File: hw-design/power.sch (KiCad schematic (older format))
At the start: 9 parts

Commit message: Routing
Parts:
- D5, D6: renamed from D?; footprint (none) -> w_smd_diode:do214ac
- U4: renamed from U?; footprint TO_SOT_Packages_SMD:SOT-223 -> linear:SOT223
- gave numbers to parts that had none: 6
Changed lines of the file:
@@
 $EndDescr
 $Comp
-L CP C?
+L CP C15
 U 1 1 5723EAD0
 P 8175 3300
-F 0 "C?" H 8200 3400 50  0000 L CNN
+F 0 "C15" H 8200 3400 50  0000 L CNN
 F 1 "10µF" H 8200 3200 50  0000 L CNN
 F 2 "w_smd_cap:c_tant_B" H 8213 3150 30  0001 C CNN
@@
 	8175 3025 8175 3150
 $Comp
-L MCP73833 U?
+L MCP73833 U3
 U 1 1 5723EAD1
 P 5450 3525
-F 0 "U?" H 5500 3625 60  0000 C CNN
+F 0 "U3" H 5500 3625 60  0000 C CNN
 F 1 "MCP73833" V 5400 3525 60  0000 C CNN
 F 2 "ref-packages:MSOP10" H 5500 3575 60  0001 C CNN
@@
 $EndComp
 $Comp
-L CP C?
+L CP C14
 U 1 1 5723EAD2
 P 7225 3300
-F 0 "C?" H 7343 3346 50  0000 L CNN
+F 0 "C14" H 7343 3346 50  0000 L CNN
 F 1 "10µF" H 7343 3254 50  0000 L CNN
 F 2 "w_smd_cap:c_tant_B" H 7263 3150 30  0001 C CNN
@@
 	3225 3325 4850 3325
 $Comp
-L CP C?
+L CP C13
 U 1 1 5723EAD3
 P 3400 3600
-F 0 "C?" H 3518 3646 50  0000 L CNN
+F 0 "C13" H 3518 3646 50  0000 L CNN
 F 1 "10µF" H 3518 3554 50  0000 L CNN
 F 2 "w_smd_cap:c_tant_B" H 3438 3450 30  0001 C CNN
@@
 	3400 3325 3400 3450
 $Comp
-L +5V #PWR?
+L +5V #PWR022
 U 1 1 5723EAD4
 P 3225 3325
-F 0 "#PWR?" H 3225 3175 50  0001 C CNN
+F 0 "#PWR022" H 3225 3175 50  0001 C CNN
 F 1 "+5V" H 3225 3465 50  0000 C CNN
 F 2 "" H 3225 3325 60  0000 C CNN
@@
 Connection ~ 3400 3325
 $Comp
-L GND #PWR?
+L GND #PWR023
 U 1 1 5723EAD5
 P 3400 3825
-F 0 "#PWR?" H 3400 3575 50  0001 C CNN
+F 0 "#PWR023" H 3400 3575 50  0001 C CNN
 F 1 "GND" H 3400 3675 50  0000 C CNN
 F 2 "" H 3400 3825 60  0000 C CNN
@@
 	4175 3625 4850 3625
 $Comp
-L GND #PWR?
+L GND #PWR024
 U 1 1 5723EAD6
 P 4775 4125
-F 0 "#PWR?" H 4775 3875 50  0001 C CNN
+F 0 "#PWR024" H 4775 3875 50  0001 C CNN
 F 1 "GND" H 4775 3975 50  0000 C CNN
 F 2 "" H 4775 4125 60  0000 C CNN
@@
 	4775 3725 4775 4125
 $Comp
-L GND #PWR?
+L GND #PWR025
 U 1 1 5723EAD7
 P 7750 3750
-F 0 "#PWR?" H 7750 3500 50  0001 C CNN
+F 0 "#PWR025" H 7750 3500 50  0001 C CNN
 F 1 "GND" H 7750 3600 50  0000 C CNN
 F 2 "" H 7750 3750 60  0000 C CNN
@@
 Connection ~ 7750 3525
 $Comp
-L +3V3 #PWR?
+L +3V3 #PWR026
 U 1 1 5723EAD8
 P 8350 3025
-F 0 "#PWR?" H 8350 2875 50  0001 C CNN
+F 0 "#PWR026" H 8350 2875 50  0001 C CNN
 F 1 "+3V3" H 8350 3165 50  0000 C CNN
 F 2 "" H 8350 3025 60  0000 C CNN
@@
 Connection ~ 8175 3025
 $Comp
-L R R?
+L R R12
 U 1 1 5723EAD9
 P 5450 3950
-F 0 "R?" V 5530 3950 50  0000 C CNN
+F 0 "R12" V 5530 3950 50  0000 C CNN
 F 1 "3k3" V 5450 3950 50  0000 C CNN
 F 2 "w_smd_resistors:r_0603" V 5380 3950 30  0001 C CNN
@@
 300mA
 $Comp
-L CONN_01X03 P?
+L CONN_01X03 P3
 U 1 1 5723EADA
 P 6750 3425
-F 0 "P?" V 6715 3231 50  0000 R CNN
+F 0 "P3" V 6715 3231 50  0000 R CNN
 F 1 "CONN_01X03" V 6623 3231 50  0000 R CNN
 F 2 "w_pin_strip:pin_strip_3" H 6750 3425 60  0001 C CNN
@@
 Connection ~ 6125 3325
 $Comp
-L GND #PWR?
+L GND #PWR027
 U 1 1 5723EADB
 P 6550 3575
-F 0 "#PWR?" H 6550 3325 50  0001 C CNN
+F 0 "#PWR027" H 6550 3325 50  0001 C CNN
 F 1 "GND" H 6644 3538 50  0000 L CNN
 F 2 "" H 6550 3575 60  0000 C CNN
@@
 	6550 3575 6550 3525
 $Comp
-L AP111733 U?
+L AP111733 U4
 U 1 1 57241BB2
 P 7750 3025
-F 0 "U?" H 7750 3392 50  0000 C CNN
+F 0 "U4" H 7750 3392 50  0000 C CNN
 F 1 "AP111733" H 7750 3301 50  0000 C CNN
-F 2 "TO_SOT_Packages_SMD:SOT-223" H 7750 2675 50  0001 C CNN
+F 2 "linear:SOT223" H 7750 2675 50  0001 C CNN
 F 3 "" H 7850 2775 50  0000 C CNN
 	1    7750 3025
@@
 	6300 3425 6550 3425
 $Comp
-L D_Schottky D?
+L D_Schottky D6
 U 1 1 57249FBF
 P 6400 3025
-F 0 "D?" H 6400 2809 50  0000 C CNN
+F 0 "D6" H 6400 2809 50  0000 C CNN
 F 1 "D_Schottky" H 6400 2900 50  0000 C CNN
-F 2 "" H 6400 3025 50  0000 C CNN
+F 2 "w_smd_diode:do214ac" H 6400 3025 50  0001 C CNN
 F 3 "" H 6400 3025 50  0000 C CNN
 	1    6400 3025
@@
 	5600 3025 6250 3025
 $Comp
-L D_Schottky D?
+L D_Schottky D5
 U 1 1 5724AD72
 P 6400 2700
-F 0 "D?" H 6400 2484 50  0000 C CNN
+F 0 "D5" H 6400 2484 50  0000 C CNN
 F 1 "D_Schottky" H 6400 2575 50  0000 C CNN
-F 2 "" H 6400 2700 50  0000 C CNN
+F 2 "w_smd_diode:do214ac" H 6400 2700 50  0001 C CNN
 F 3 "" H 6400 2700 50  0000 C CNN
 	1    6400 2700
@@
 sense
 $Comp
-L +BATT #PWR?
+L +BATT #PWR028
 U 1 1 572542F4
 P 6125 2950
-F 0 "#PWR?" H 6125 2800 50  0001 C CNN
+F 0 "#PWR028" H 6125 2800 50  0001 C CNN
 F 1 "+BATT" H 6140 3123 50  0000 C CNN
 F 2 "" H 6125 2950 50  0000 C CNN

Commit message: Mounting holes for additional wheels or whatever
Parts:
- removed D6: D_Schottky, w_smd_diode:do214ac, symbol D_Schottky
- D5: footprint w_smd_diode:do214ac -> iwasz:sod123-pins21
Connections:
- net +BATT: now also C14.1, D5.1 (K), U4.3 (VI)
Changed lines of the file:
@@
 	3400 3325 3400 3450
 $Comp
-L +5V #PWR022
+L +5V #PWR22
 U 1 1 5723EAD4
 P 3225 3325
-F 0 "#PWR022" H 3225 3175 50  0001 C CNN
+F 0 "#PWR22" H 3225 3175 50  0001 C CNN
 F 1 "+5V" H 3225 3465 50  0000 C CNN
 F 2 "" H 3225 3325 60  0000 C CNN
@@
 Connection ~ 3400 3325
 $Comp
-L GND #PWR023
+L GND #PWR23
 U 1 1 5723EAD5
 P 3400 3825
-F 0 "#PWR023" H 3400 3575 50  0001 C CNN
+F 0 "#PWR23" H 3400 3575 50  0001 C CNN
 F 1 "GND" H 3400 3675 50  0000 C CNN
 F 2 "" H 3400 3825 60  0000 C CNN
@@
 	4175 3625 4850 3625
 $Comp
-L GND #PWR024
+L GND #PWR24
 U 1 1 5723EAD6
 P 4775 4125
-F 0 "#PWR024" H 4775 3875 50  0001 C CNN
+F 0 "#PWR24" H 4775 3875 50  0001 C CNN
 F 1 "GND" H 4775 3975 50  0000 C CNN
 F 2 "" H 4775 4125 60  0000 C CNN
@@
 	4775 3725 4775 4125
 $Comp
-L GND #PWR025
+L GND #PWR27
 U 1 1 5723EAD7
 P 7750 3750
-F 0 "#PWR025" H 7750 3500 50  0001 C CNN
+F 0 "#PWR27" H 7750 3500 50  0001 C CNN
 F 1 "GND" H 7750 3600 50  0000 C CNN
 F 2 "" H 7750 3750 60  0000 C CNN
@@
 Connection ~ 7750 3525
 $Comp
-L +3V3 #PWR026
+L +3V3 #PWR28
 U 1 1 5723EAD8
 P 8350 3025
-F 0 "#PWR026" H 8350 2875 50  0001 C CNN
+F 0 "#PWR28" H 8350 2875 50  0001 C CNN
 F 1 "+3V3" H 8350 3165 50  0000 C CNN
 F 2 "" H 8350 3025 60  0000 C CNN
@@
 Connection ~ 6125 3325
 $Comp
-L GND #PWR027
+L GND #PWR26
 U 1 1 5723EADB
 P 6550 3575
-F 0 "#PWR027" H 6550 3325 50  0001 C CNN
+F 0 "#PWR26" H 6550 3325 50  0001 C CNN
 F 1 "GND" H 6644 3538 50  0000 L CNN
 F 2 "" H 6550 3575 60  0000 C CNN
@@
 	6000 3325 6550 3325
 Wire Wire Line
-	6550 3025 7450 3025
+	5600 3025 7450 3025
 Wire Wire Line
 	6550 3575 6550 3525
@@
 	6300 3425 6550 3425
 $Comp
-L D_Schottky D6
-U 1 1 57249FBF
-P 6400 3025
-F 0 "D6" H 6400 2809 50  0000 C CNN
-F 1 "D_Schottky" H 6400 2900 50  0000 C CNN
-F 2 "w_smd_diode:do214ac" H 6400 3025 50  0001 C CNN
-F 3 "" H 6400 3025 50  0000 C CNN
-	1    6400 3025
-	-1   0    0    1
-$EndComp
-Wire Wire Line
-	5600 3025 6250 3025
-$Comp
 L D_Schottky D5
 U 1 1 5724AD72
@@
 F 0 "D5" H 6400 2484 50  0000 C CNN
 F 1 "D_Schottky" H 6400 2575 50  0000 C CNN
-F 2 "w_smd_diode:do214ac" H 6400 2700 50  0001 C CNN
+F 2 "iwasz:sod123-pins21" H 6400 2700 50  0001 C CNN
 F 3 "" H 6400 2700 50  0000 C CNN
 	1    6400 2700
@@
 sense
 $Comp
-L +BATT #PWR028
+L +BATT #PWR25
 U 1 1 572542F4
 P 6125 2950
-F 0 "#PWR028" H 6125 2800 50  0001 C CNN
+F 0 "#PWR25" H 6125 2800 50  0001 C CNN
 F 1 "+BATT" H 6140 3123 50  0000 C CNN
 F 2 "" H 6125 2950 50  0000 C CNN

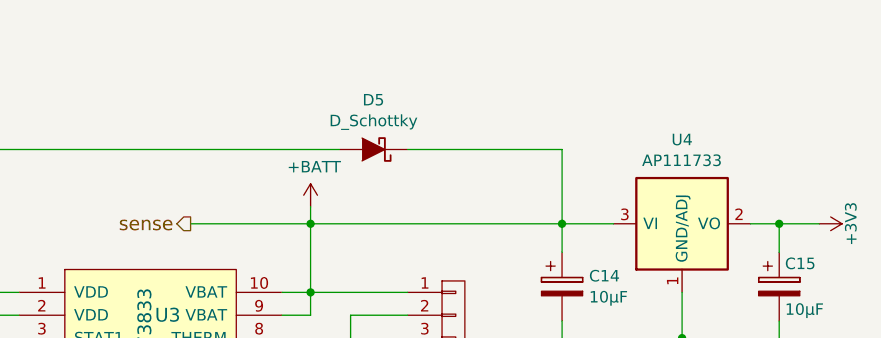
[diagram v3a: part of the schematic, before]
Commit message: Docs, PCB modified (problems with RF and low speed oscillator)
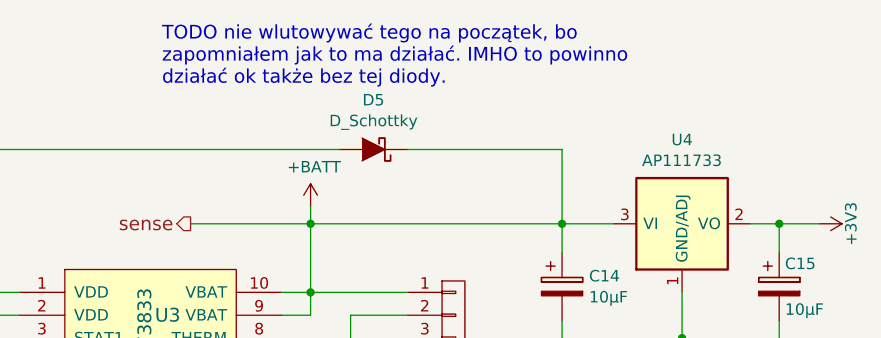
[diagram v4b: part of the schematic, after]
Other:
- note added: "TODO nie wlutowywać tego na początek, bo\nzapomniałem jak to ma działać. IMHO to powinno\ndziałać ok także bez tej diody."
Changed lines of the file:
@@
 	3400 3325 3400 3450
 $Comp
-L +5V #PWR22
+L +5V #PWR022
 U 1 1 5723EAD4
 P 3225 3325
-F 0 "#PWR22" H 3225 3175 50  0001 C CNN
+F 0 "#PWR022" H 3225 3175 50  0001 C CNN
 F 1 "+5V" H 3225 3465 50  0000 C CNN
 F 2 "" H 3225 3325 60  0000 C CNN
@@
 Connection ~ 3400 3325
 $Comp
-L GND #PWR23
+L GND #PWR023
 U 1 1 5723EAD5
 P 3400 3825
-F 0 "#PWR23" H 3400 3575 50  0001 C CNN
+F 0 "#PWR023" H 3400 3575 50  0001 C CNN
 F 1 "GND" H 3400 3675 50  0000 C CNN
 F 2 "" H 3400 3825 60  0000 C CNN
@@
 	4175 3625 4850 3625
 $Comp
-L GND #PWR24
+L GND #PWR024
 U 1 1 5723EAD6
 P 4775 4125
-F 0 "#PWR24" H 4775 3875 50  0001 C CNN
+F 0 "#PWR024" H 4775 3875 50  0001 C CNN
 F 1 "GND" H 4775 3975 50  0000 C CNN
 F 2 "" H 4775 4125 60  0000 C CNN
@@
 	4775 3725 4775 4125
 $Comp
-L GND #PWR27
+L GND #PWR025
 U 1 1 5723EAD7
 P 7750 3750
-F 0 "#PWR27" H 7750 3500 50  0001 C CNN
+F 0 "#PWR025" H 7750 3500 50  0001 C CNN
 F 1 "GND" H 7750 3600 50  0000 C CNN
 F 2 "" H 7750 3750 60  0000 C CNN
@@
 Connection ~ 7750 3525
 $Comp
-L +3V3 #PWR28
+L +3V3 #PWR026
 U 1 1 5723EAD8
 P 8350 3025
-F 0 "#PWR28" H 8350 2875 50  0001 C CNN
+F 0 "#PWR026" H 8350 2875 50  0001 C CNN
 F 1 "+3V3" H 8350 3165 50  0000 C CNN
 F 2 "" H 8350 3025 60  0000 C CNN
@@
 Connection ~ 6125 3325
 $Comp
-L GND #PWR26
+L GND #PWR027
 U 1 1 5723EADB
 P 6550 3575
-F 0 "#PWR26" H 6550 3325 50  0001 C CNN
+F 0 "#PWR027" H 6550 3325 50  0001 C CNN
 F 1 "GND" H 6644 3538 50  0000 L CNN
 F 2 "" H 6550 3575 60  0000 C CNN
@@
 sense
 $Comp
-L +BATT #PWR25
+L +BATT #PWR028
 U 1 1 572542F4
 P 6125 2950
-F 0 "#PWR25" H 6125 2800 50  0001 C CNN
+F 0 "#PWR028" H 6125 2800 50  0001 C CNN
 F 1 "+BATT" H 6140 3123 50  0000 C CNN
 F 2 "" H 6125 2950 50  0000 C CNN
@@
 	1    0    0    -1
 $EndComp
+Text Notes 5475 2425 0    60   ~ 0
+TODO nie wlutowywać tego na początek, bo\nzapomniałem jak to ma działać. IMHO to powinno\ndziałać ok także bez tej diody.
 $EndSCHEMATC

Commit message: Gerbery 1.1
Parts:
- added P10: CONN_01X02, w_pin_strip:pin_strip_2, symbol CONN_01X02
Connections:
- net +BATT: now also P10.1 (P1); no longer P3.1 (P1), U3.10 (VBAT), U3.9 (VBAT)
- new net: P10.2 (P2), P3.1 (P1), U3.10 (VBAT), U3.9 (VBAT)
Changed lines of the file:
@@
 	3400 3325 3400 3450
 $Comp
-L +5V #PWR022
+L +5V #PWR22
 U 1 1 5723EAD4
 P 3225 3325
-F 0 "#PWR022" H 3225 3175 50  0001 C CNN
+F 0 "#PWR22" H 3225 3175 50  0001 C CNN
 F 1 "+5V" H 3225 3465 50  0000 C CNN
 F 2 "" H 3225 3325 60  0000 C CNN
@@
 Connection ~ 3400 3325
 $Comp
-L GND #PWR023
+L GND #PWR23
 U 1 1 5723EAD5
 P 3400 3825
-F 0 "#PWR023" H 3400 3575 50  0001 C CNN
+F 0 "#PWR23" H 3400 3575 50  0001 C CNN
 F 1 "GND" H 3400 3675 50  0000 C CNN
 F 2 "" H 3400 3825 60  0000 C CNN
@@
 	4175 3625 4850 3625
 $Comp
-L GND #PWR024
+L GND #PWR24
 U 1 1 5723EAD6
 P 4775 4125
-F 0 "#PWR024" H 4775 3875 50  0001 C CNN
+F 0 "#PWR24" H 4775 3875 50  0001 C CNN
 F 1 "GND" H 4775 3975 50  0000 C CNN
 F 2 "" H 4775 4125 60  0000 C CNN
@@
 	4775 3725 4775 4125
 $Comp
-L GND #PWR025
+L GND #PWR27
 U 1 1 5723EAD7
 P 7750 3750
-F 0 "#PWR025" H 7750 3500 50  0001 C CNN
+F 0 "#PWR27" H 7750 3500 50  0001 C CNN
 F 1 "GND" H 7750 3600 50  0000 C CNN
 F 2 "" H 7750 3750 60  0000 C CNN
@@
 Connection ~ 7750 3525
 $Comp
-L +3V3 #PWR026
+L +3V3 #PWR28
 U 1 1 5723EAD8
 P 8350 3025
-F 0 "#PWR026" H 8350 2875 50  0001 C CNN
+F 0 "#PWR28" H 8350 2875 50  0001 C CNN
 F 1 "+3V3" H 8350 3165 50  0000 C CNN
 F 2 "" H 8350 3025 60  0000 C CNN
@@
 Connection ~ 6125 3325
 $Comp
-L GND #PWR027
+L GND #PWR26
 U 1 1 5723EADB
 P 6550 3575
-F 0 "#PWR027" H 6550 3325 50  0001 C CNN
+F 0 "#PWR26" H 6550 3325 50  0001 C CNN
 F 1 "GND" H 6644 3538 50  0000 L CNN
 F 2 "" H 6550 3575 60  0000 C CNN
@@
 Connection ~ 7225 3025
 Wire Wire Line
-	6125 2950 6125 3425
+	6125 2950 6125 3125
+Wire Wire Line
+	6125 3225 6125 3425
 Wire Wire Line
 	6300 3425 6300 3525
-Wire Wire Line
-	6000 3325 6550 3325
 Wire Wire Line
 	5600 3025 7450 3025
@@
 sense
 $Comp
-L +BATT #PWR028
+L +BATT #PWR25
 U 1 1 572542F4
 P 6125 2950
-F 0 "#PWR028" H 6125 2800 50  0001 C CNN
+F 0 "#PWR25" H 6125 2800 50  0001 C CNN
 F 1 "+BATT" H 6140 3123 50  0000 C CNN
 F 2 "" H 6125 2950 50  0000 C CNN
@@
 Text Notes 5475 2425 0    60   ~ 0
 TODO nie wlutowywać tego na początek, bo\nzapomniałem jak to ma działać. IMHO to powinno\ndziałać ok także bez tej diody.
+$Comp
+L CONN_01X02 P10
+U 1 1 577EA8A3
+P 6350 3175
+F 0 "P10" H 6428 3216 50  0000 L CNN
+F 1 "CONN_01X02" H 6428 3125 50  0000 L CNN
+F 2 "w_pin_strip:pin_strip_2" V 6178 3037 50  0001 R CNN
+F 3 "" H 6350 3175 50  0000 C CNN
+	1    6350 3175
+	1    0    0    -1
+$EndComp
+Wire Wire Line
+	6000 3325 6550 3325
+Wire Wire Line
+	6125 3125 6150 3125
+Wire Wire Line
+	6125 3225 6150 3225
 $EndSCHEMATC

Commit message: BT turned of/on #define
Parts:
- U3: Datasheet2 (none) -> http://pl.rs-online.com/web/p/uklady-ladowania-akumulatorow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
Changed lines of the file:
@@
 F 2 "ref-packages:MSOP10" H 5500 3575 60  0001 C CNN
 F 3 "http://pl.farnell.com/microchip/mcp73833-fci-un/ic-charge-control-li-ion-1a-msop/dp/1605576" H 5500 3575 60  0001 C CNN
+F 4 "http://pl.rs-online.com/web/p/uklady-ladowania-akumulatorow/7240523/" H 5450 3525 60  0001 C CNN "Datasheet2"
 	1    5450 3525
 	1    0    0    -1

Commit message: version 1.1 works.
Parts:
- removed D5: D_Schottky, iwasz:sod123-pins21, symbol D_Schottky
- added R18: 10k, w_smd_resistors:r_0603, symbol R
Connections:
- net GND: now also R18.1
- net at P3.2 (P2), U3.8 (THERM): now also R18.2
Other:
- note added: "300mA, 4k7 = 210mA, Ireg = 1000V/Rreg\nGdy bateria nie ma termometru, to wlutować R18"
- note added: "opt"
- note removed: "300mA"
- note removed: "TODO nie wlutowywać tego na początek, bo\nzapomniałem jak to ma działać. IMHO to powinno\ndziałać ok także bez tej diody."
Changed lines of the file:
@@
 Wire Wire Line
 	4675 3425 4850 3425
-Wire Wire Line
-	4675 2700 4675 3425
 Connection ~ 4675 3325
 Wire Wire Line
@@
 	4775 3950 5300 3950
 Connection ~ 4775 3950
-Text Notes 5300 4150 0    60   ~ 0
-300mA
+Text Notes 4375 4575 0    60   ~ 0
+300mA, 4k7 = 210mA, Ireg = 1000V/Rreg\nGdy bateria nie ma termometru, to wlutować R18
 $Comp
 L CONN_01X03 P3
@@
 L GND #PWR26
 U 1 1 5723EADB
-P 6550 3575
-F 0 "#PWR26" H 6550 3325 50  0001 C CNN
-F 1 "GND" H 6644 3538 50  0000 L CNN
-F 2 "" H 6550 3575 60  0000 C CNN
-F 3 "" H 6550 3575 60  0000 C CNN
-	1    6550 3575
+P 6550 4025
+F 0 "#PWR26" H 6550 3775 50  0001 C CNN
+F 1 "GND" H 6644 3988 50  0000 L CNN
+F 2 "" H 6550 4025 60  0000 C CNN
+F 3 "" H 6550 4025 60  0000 C CNN
+	1    6550 4025
 	1    0    0    -1
 $EndComp
@@
 	6125 3225 6125 3425
 Wire Wire Line
-	6300 3425 6300 3525
+	6300 3425 6300 3575
 Wire Wire Line
-	5600 3025 7450 3025
-Wire Wire Line
-	6550 3575 6550 3525
+	6550 3525 6550 4025
 $Comp
 L AP111733 U4
@@
 	1    0    0    -1
 $EndComp
-Wire Wire Line
-	7225 2700 7225 3150
 NoConn ~ 6000 3625
 Wire Wire Line
 	6300 3425 6550 3425
-$Comp
-L D_Schottky D5
-U 1 1 5724AD72
-P 6400 2700
-F 0 "D5" H 6400 2484 50  0000 C CNN
-F 1 "D_Schottky" H 6400 2575 50  0000 C CNN
-F 2 "iwasz:sod123-pins21" H 6400 2700 50  0001 C CNN
-F 3 "http://pl.farnell.com/multicomp/1n4148ws/diode-h-speed-100v-0-15a-sod323/dp/1466524" H 6400 2700 50  0001 C CNN
-	1    6400 2700
-	-1   0    0    1
-$EndComp
-Wire Wire Line
-	4675 2700 6250 2700
-Wire Wire Line
-	6550 2700 7225 2700
 Connection ~ 6125 3025
 Text HLabel 4175 3525 0    60   Output ~ 0
@@
 Text HLabel 4175 3625 0    60   Output ~ 0
 complete
-Text HLabel 5600 3025 0    60   Output ~ 0
+Text HLabel 7225 2850 1    60   Output ~ 0
 sense
 $Comp
@@
 	1    0    0    -1
 $EndComp
-Text Notes 5475 2425 0    60   ~ 0
-TODO nie wlutowywać tego na początek, bo\nzapomniałem jak to ma działać. IMHO to powinno\ndziałać ok także bez tej diody.
 $Comp
 L CONN_01X02 P10
@@
 Wire Wire Line
 	6125 3225 6150 3225
+$Comp
+L R R18
+U 1 1 57D567E4
+P 6300 3725
+F 0 "R18" V 6380 3725 50  0000 C CNN
+F 1 "10k" V 6300 3725 50  0000 C CNN
+F 2 "w_smd_resistors:r_0603" V 6230 3725 30  0001 C CNN
+F 3 "" H 6300 3725 30  0000 C CNN
+	1    6300 3725
+	-1   0    0    1
+$EndComp
+Wire Wire Line
+	6300 3875 6550 3875
+Connection ~ 6550 3875
+Connection ~ 6300 3525
+Text Notes 6425 3800 1    60   ~ 0
+opt
+Wire Wire Line
+	6125 3025 7450 3025
+Wire Wire Line
+	7225 2850 7225 3150
+Wire Wire Line
+	4675 3425 4675 3325
 $EndSCHEMATC
